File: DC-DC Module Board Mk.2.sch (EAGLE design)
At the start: 50 parts, among them J1 AVR_ICSP, P1 87833-04_S, Q1 SUM90P10-19L, Q2 ASFL1, Q3 MMBT540LT1SMD, U1 ATMEGA168, U2 CHB350, U4 LTV816S, X1 5566-2, X2 5566-2, X3 5566-2

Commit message: updated brick board to new half brick
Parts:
- removed C15, C16: 10nF, resistor:C-USC0603
- removed C17, C18, C21: 100nF, resistor:C-USC0603
- removed FB1: (no value), microbuilder:FERRITE
- removed J1: AVR_ICSP, SparkFun:AVR_SPI_PRG_62X3_LOCK
- removed LED5: YELLOW, SparkFun:LED0603
- removed LED6: GREEN, SparkFun:LED0603
- removed LED7: BLUE, SparkFun:LED0603
- removed Q2: ASFL1, crystal:ASFL1
- removed R15: 10k, resistor:R-US_R0603
- removed R16, R17, R18: 350, resistor:R-US_R0603
- removed R19, R20: 3.3k, resistor:R-US_R0603
- removed R21: 10k, pot:TRIM_US-SM-42/43W
- removed S1: (no value), SparkFun:TAC_SWITCHSMD
- removed U1: ATMEGA168, SparkFun:ATMEGA168
- removed U2: CHB350, Custom_Components:CHB350-24V
- added U$1: BRICK_DC-DC_CONVERTER, PowerComponents:BRICK_DC-DC_CONVERTER
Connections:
- removed net A0: U1.PD0(RXD)
- removed net A1: U1.PD1(TXD)
- removed net A2: U1.PD2(INT0)
- removed net AREF: C16.1, U1.AREF
- removed net CLK: Q2.FO, U1.PB6(XTAL1/TOSC1)
- removed net I24_MEA: U1.PC3(ADC3)
- removed net MISO: J1.1, U1.PB4(MISO)
- removed net MOSI: J1.4, U1.PB3(MOSI/OC2)
- removed net N$16: FB1.P$2, U1.AVCC
- removed net N$19: R21.S, U2.TRIM
- removed net N$20: LED5.A, R16.1
- removed net N$21: LED6.A, R17.1
- removed net N$25: LED7.A, R18.1
- removed net RST: C15.1, J1.5, R15.1, S1.3, S1.4, U1.PC6(/RESET)
- removed net SCK: J1.3, U1.PB5(SCK)
- removed net TEMP_OUT: U1.PC2(ADC2)
- removed net TEST1: R16.2, U1.PD5(T1)
- removed net TEST2: R17.2, U1.PD6(AIN0)
- removed net TEST3: R18.2, U1.PD7(AIN1)
- removed net V24_MEA: U1.PC0(ADC0)
- net +5V: no longer C17.1, C18.1, C21.1, FB1.P$1, J1.2, Q2.VCC, R15.2, R19.2, R20.2, U1.VCC@1, U1.VCC@2
- net EN: no longer U2.EN
- net ENABLE: no longer U1.PD4(XCK/T0)
- net GND: now also U$1.-S, U$1.-VOUT; no longer C15.2, C16.2, C17.2, C18.2, C21.2, J1.6, LED5.C, LED6.C, LED7.C, Q2.GND, R21.E, S1.1, S1.2, U1.AGND, U1.GND@1, U1.GND@2, U2.GND, U2.SENSE-
- net GND1: now also U$1.-VIN; no longer U2.VIN-
- net N$6: now also U$1.+VIN; no longer U2.VIN+
- net SCL: no longer R19.1, U1.PC5(ADC5/SCL)
- net SDA: no longer R20.1, U1.PC4(ADC4/SDA)
- net V+: now also U$1.+S, U$1.+VOUT; no longer R21.A, U2.SENSE+, U2.VOUT
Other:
- note removed: "C:/Users/Clayton Kleppinger/Dropbox/IEEE ROV 2012/Electronics/DC-DC Module Board/purdue-logo.bmp"

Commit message: addressing and labels
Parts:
- removed C13, C19: 100nF, resistor:C-USC0603
- removed P1: 87833-04_S, con-molex-milli-grid:87833-04_S
- removed Q3: MMBT540LT1SMD, transistor-pnp:MMBT540LT1SMD
- removed R1: 1k, resistor:R-US_R0603
- removed R22, R23, R24: 10k, resistor:R-US_R0603
- removed U4: LTV816S, optocoupler:LTV816S
- removed X1, X2, X3: 5566-2, con-molex:5566-2
- added R5, R7: 10, resistor:R-US_R0603
- added R6: 0, resistor:R-US_R0603
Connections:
- removed net +24V: C19.1, X2-2.S, X3-2.S
- removed net +5V: P1-3.P
- removed net EN: R22.1, R24.1
- removed net ENABLE: R1.1
- removed net N$22: Q3.C, R24.2
- removed net N$23: R23.1, U4.COL
- removed net N$24: Q3.B, R23.2
- new net ADRS00A: R7.2, U$1.SA0
- new net ADRS00B: R5.2, U$1.SA1
- new net ALERT: U$1.SMBALERT
- new net PG: U$1.PG
- net GND: now also R5.1, R7.1; no longer C19.2, P1-4.P, U4.C, X2-1.S, X3-1.S
- net GND1: now also R6.1; no longer C13.2, R22.2, U4.EMIT, X1-1.S
- net N$1: now also R6.2, U$1.ON/OFF1; no longer R1.2, U4.A
- net N$6: no longer Q3.E
- net SCL: now also U$1.SCL; no longer P1-1.P
- net SDA: now also U$1.SDA; no longer P1-2.P
- net VCC: no longer C13.1, X1-2.S
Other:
- note added: "address 00"

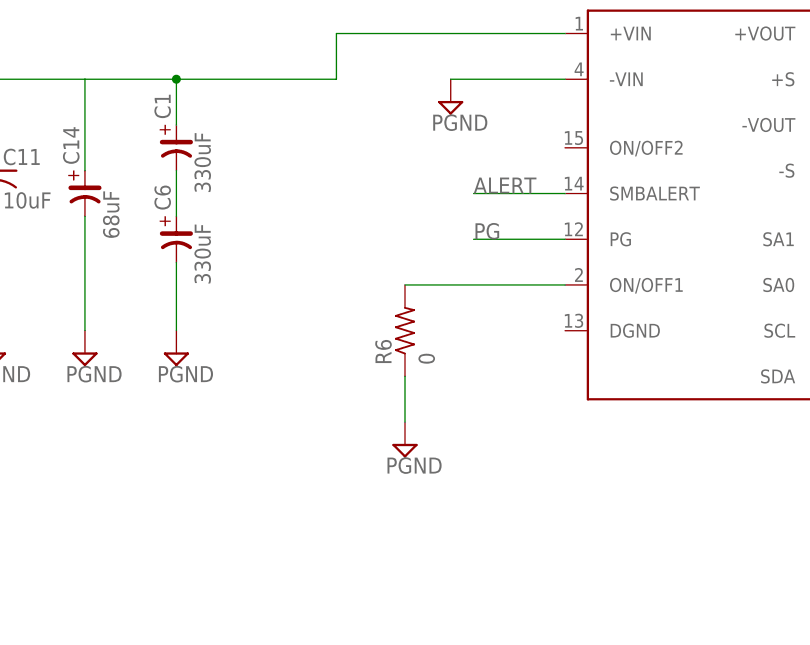
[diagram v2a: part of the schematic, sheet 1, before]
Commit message: added LEDs to smbalert and pg
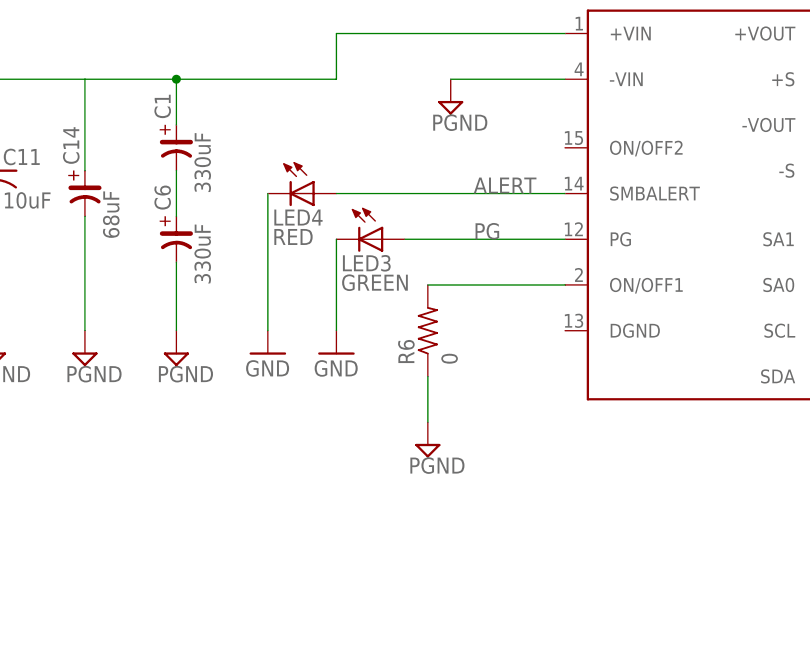
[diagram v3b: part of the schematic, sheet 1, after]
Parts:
- added LED3: GREEN, SparkFun:LED0603
- added LED4: RED, SparkFun:LED0603
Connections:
- net ALERT: now also LED4.A
- net GND: now also LED3.C, LED4.C
- net PG: now also LED3.A
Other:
- moved on the sheet: R6
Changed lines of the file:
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@@
 <attribute name="PARTNO" value="1.00MHCT-ND"/>
 </part>
+<part name="LED3" library="SparkFun" deviceset="LED" device="0603" value="GREEN">
+<attribute name="BOM" value="INCLUDE"/>
+<attribute name="PARTNO" value="160-1446-1-ND"/>
+</part>
+<part name="LED4" library="SparkFun" deviceset="LED" device="0603" value="RED">
+<attribute name="BOM" value="INCLUDE"/>
+<attribute name="PARTNO" value="160-1446-1-ND"/>
+</part>
+<part name="GND5" library="supply1" deviceset="GND" device=""/>
+<part name="GND6" library="supply1" deviceset="GND" device=""/>
 </parts>
 <sheets>
@@
 <instance part="GND2" gate="1" x="160.02" y="114.3"/>
 <instance part="U$1" gate="G$1" x="129.54" y="124.46"/>
-<instance part="SUPPLY7" gate="G$1" x="96.52" y="86.36"/>
+<instance part="SUPPLY7" gate="G$1" x="99.06" y="86.36"/>
 <instance part="GND1" gate="1" x="180.34" y="86.36"/>
 <instance part="R5" gate="G$1" x="180.34" y="99.06" rot="R90">
@@
 <attribute name="BOM" value="INCLUDE" x="180.34" y="99.06" size="0.0254" layer="96" font="vector" display="off"/>
 </instance>
-<instance part="R6" gate="G$1" x="96.52" y="99.06" rot="R90">
-<attribute name="PARTNO" value="1.00MHCT-ND" x="96.52" y="99.06" size="0.0254" layer="96" font="vector" display="off"/>
-<attribute name="BOM" value="INCLUDE" x="96.52" y="99.06" size="0.0254" layer="96" font="vector" display="off"/>
+<instance part="R6" gate="G$1" x="99.06" y="99.06" rot="R90">
+<attribute name="PARTNO" value="1.00MHCT-ND" x="99.06" y="99.06" size="0.0254" layer="96" font="vector" display="off"/>
+<attribute name="BOM" value="INCLUDE" x="99.06" y="99.06" size="0.0254" layer="96" font="vector" display="off"/>
 </instance>
 <instance part="R7" gate="G$1" x="167.64" y="99.06" rot="R90">
@@
 <attribute name="BOM" value="INCLUDE" x="167.64" y="99.06" size="0.0254" layer="96" font="vector" display="off"/>
 </instance>
+<instance part="LED3" gate="G$1" x="93.98" y="109.22" rot="R270">
+<attribute name="PARTNO" value="160-1446-1-ND" x="93.98" y="109.22" size="0.0254" layer="96" font="vector" rot="R270" display="off"/>
+<attribute name="BOM" value="INCLUDE" x="93.98" y="109.22" size="0.0254" layer="96" font="vector" rot="R270" display="off"/>
+</instance>
+<instance part="LED4" gate="G$1" x="86.36" y="114.3" rot="R270">
+<attribute name="PARTNO" value="160-1446-1-ND" x="86.36" y="114.3" size="0.0254" layer="96" font="vector" rot="R270" display="off"/>
+<attribute name="BOM" value="INCLUDE" x="86.36" y="114.3" size="0.0254" layer="96" font="vector" rot="R270" display="off"/>
+</instance>
+<instance part="GND5" gate="1" x="81.28" y="96.52"/>
+<instance part="GND6" gate="1" x="88.9" y="96.52"/>
 </instances>
 <busses>
@@
 <junction x="180.34" y="93.98"/>
 <pinref part="R7" gate="G$1" pin="1"/>
+</segment>
+<segment>
+<pinref part="LED4" gate="G$1" pin="C"/>
+<wire x1="81.28" y1="114.3" x2="81.28" y2="99.06" width="0.1524" layer="91"/>
+<pinref part="GND5" gate="1" pin="GND"/>
+</segment>
+<segment>
+<pinref part="LED3" gate="G$1" pin="C"/>
+<wire x1="88.9" y1="109.22" x2="88.9" y2="99.06" width="0.1524" layer="91"/>
+<pinref part="GND6" gate="1" pin="GND"/>
 </segment>
 </net>
@@
 <segment>
 <pinref part="SUPPLY7" gate="G$1" pin="GND1"/>
-<wire x1="96.52" y1="93.98" x2="96.52" y2="88.9" width="0.1524" layer="91"/>
+<wire x1="99.06" y1="93.98" x2="99.06" y2="88.9" width="0.1524" layer="91"/>
 <pinref part="R6" gate="G$1" pin="1"/>
 </segment>
@@
 <segment>
 <pinref part="U$1" gate="G$1" pin="ON/OFF1"/>
-<wire x1="114.3" y1="104.14" x2="96.52" y2="104.14" width="0.1524" layer="91"/>
+<wire x1="114.3" y1="104.14" x2="99.06" y2="104.14" width="0.1524" layer="91"/>
 <pinref part="R6" gate="G$1" pin="2"/>
 </segment>
@@
 <segment>
 <pinref part="U$1" gate="G$1" pin="SMBALERT"/>
-<wire x1="114.3" y1="114.3" x2="104.14" y2="114.3" width="0.1524" layer="91"/>
 <label x="104.14" y="114.3" size="1.778" layer="95"/>
+<pinref part="LED4" gate="G$1" pin="A"/>
+<wire x1="114.3" y1="114.3" x2="88.9" y2="114.3" width="0.1524" layer="91"/>
 </segment>
 </net>
@@
 <segment>
 <pinref part="U$1" gate="G$1" pin="PG"/>
-<wire x1="114.3" y1="109.22" x2="104.14" y2="109.22" width="0.1524" layer="91"/>
+<wire x1="114.3" y1="109.22" x2="96.52" y2="109.22" width="0.1524" layer="91"/>
 <label x="104.14" y="109.22" size="1.778" layer="95"/>
-</segment>
-</net>
+<pinref part="LED3" gate="G$1" pin="A"/>
+</segment>
+</net>

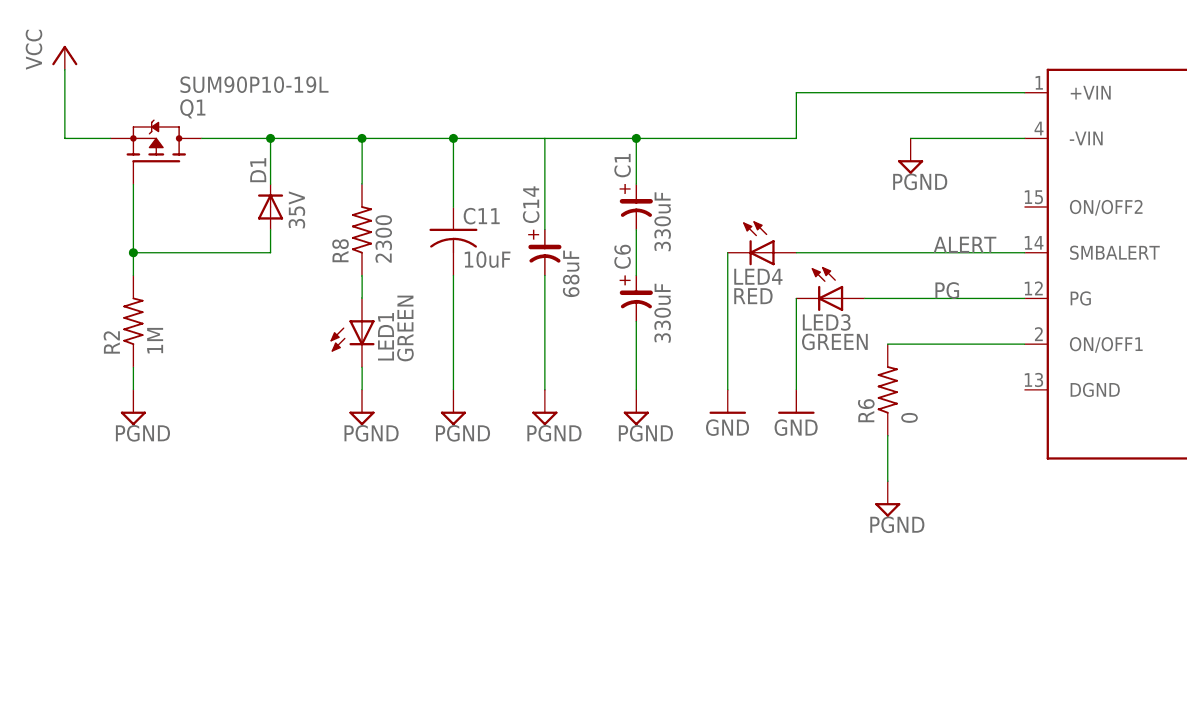
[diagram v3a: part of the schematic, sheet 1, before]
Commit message: changed PGND to GND
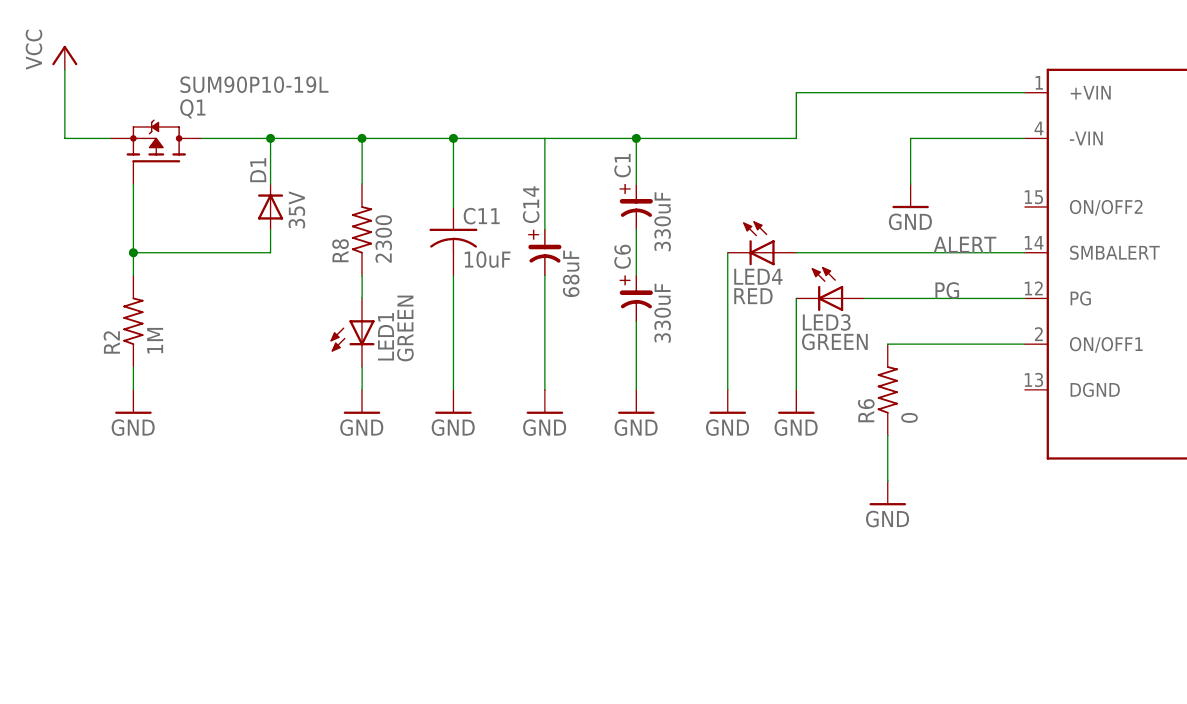
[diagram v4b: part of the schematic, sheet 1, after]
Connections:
- removed net GND1: C11.2, C14.-, C6.-, LED1.C, R2.1, R6.1, U$1.-VIN
- net GND: now also C11.2, C14.-, C6.-, LED1.C, R2.1, R6.1, U$1.-VIN
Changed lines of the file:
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@@
 <attribute name="PARTNO" value="SUM90P10-19L-E3CT-ND"/>
 </part>
-<part name="SUPPLY1" library="supply2" deviceset="GND1" device="" value="PGND"/>
-<part name="SUPPLY2" library="supply2" deviceset="GND1" device="" value="PGND"/>
-<part name="SUPPLY3" library="supply2" deviceset="GND1" device="" value="PGND"/>
-<part name="SUPPLY4" library="supply2" deviceset="GND1" device="" value="PGND"/>
-<part name="SUPPLY5" library="supply2" deviceset="GND1" device="" value="PGND"/>
 <part name="C22" library="SparkFun" deviceset="CAP_POL" device="7343" value="10uF">
 <attribute name="BOM" value="INCLUDE"/>
@@
 </part>
 <part name="GND40" library="supply1" deviceset="GND" device=""/>
-<part name="SUPPLY6" library="supply2" deviceset="GND1" device="" value="PGND"/>
 <part name="GND2" library="supply1" deviceset="GND" device=""/>
 <part name="U$1" library="PowerComponents" deviceset="BRICK_DC-DC_CONVERTER" device=""/>
-<part name="SUPPLY7" library="supply2" deviceset="GND1" device="" value="PGND"/>
 <part name="GND1" library="supply1" deviceset="GND" device=""/>
 <part name="R5" library="resistor" deviceset="R-US_" device="R0603" value="10">
@@
 <part name="GND5" library="supply1" deviceset="GND" device=""/>
 <part name="GND6" library="supply1" deviceset="GND" device=""/>
+<part name="GND7" library="supply1" deviceset="GND" device=""/>
+<part name="GND8" library="supply1" deviceset="GND" device=""/>
+<part name="GND9" library="supply1" deviceset="GND" device=""/>
+<part name="GND10" library="supply1" deviceset="GND" device=""/>
+<part name="GND11" library="supply1" deviceset="GND" device=""/>
+<part name="GND12" library="supply1" deviceset="GND" device=""/>
+<part name="GND13" library="supply1" deviceset="GND" device=""/>
 </parts>
 <sheets>
@@
 <attribute name="BOM" value="INCLUDE" x="17.78" y="124.46" size="0.0254" layer="96" font="vector" display="off"/>
 </instance>
-<instance part="SUPPLY1" gate="G$1" x="15.24" y="96.52"/>
-<instance part="SUPPLY2" gate="G$1" x="40.64" y="96.52"/>
-<instance part="SUPPLY3" gate="G$1" x="50.8" y="96.52"/>
-<instance part="SUPPLY4" gate="G$1" x="60.96" y="96.52"/>
-<instance part="SUPPLY5" gate="G$1" x="71.12" y="96.52"/>
 <instance part="C22" gate="G$1" x="208.28" y="114.3">
 <attribute name="PARTNO" value="399-3893-1-ND" x="208.28" y="114.3" size="1.778" layer="96" display="off"/>
@@
 </instance>
 <instance part="GND40" gate="1" x="228.6" y="96.52"/>
-<instance part="SUPPLY6" gate="G$1" x="101.6" y="124.46"/>
 <instance part="GND2" gate="1" x="160.02" y="114.3"/>
 <instance part="U$1" gate="G$1" x="129.54" y="124.46"/>
-<instance part="SUPPLY7" gate="G$1" x="99.06" y="86.36"/>
 <instance part="GND1" gate="1" x="180.34" y="86.36"/>
 <instance part="R5" gate="G$1" x="180.34" y="99.06" rot="R90">
@@
 <instance part="GND5" gate="1" x="81.28" y="96.52"/>
 <instance part="GND6" gate="1" x="88.9" y="96.52"/>
+<instance part="GND7" gate="1" x="71.12" y="96.52"/>
+<instance part="GND8" gate="1" x="60.96" y="96.52"/>
+<instance part="GND9" gate="1" x="50.8" y="96.52"/>
+<instance part="GND10" gate="1" x="40.64" y="96.52"/>
+<instance part="GND11" gate="1" x="15.24" y="96.52"/>
+<instance part="GND12" gate="1" x="99.06" y="86.36"/>
+<instance part="GND13" gate="1" x="101.6" y="119.38"/>
 </instances>
 <busses>
@@
 <wire x1="88.9" y1="109.22" x2="88.9" y2="99.06" width="0.1524" layer="91"/>
 <pinref part="GND6" gate="1" pin="GND"/>
+</segment>
+<segment>
+<pinref part="C6" gate="G$1" pin="-"/>
+<wire x1="71.12" y1="106.68" x2="71.12" y2="99.06" width="0.1524" layer="91"/>
+<pinref part="GND7" gate="1" pin="GND"/>
+</segment>
+<segment>
+<pinref part="C14" gate="G$1" pin="-"/>
+<wire x1="60.96" y1="111.76" x2="60.96" y2="99.06" width="0.1524" layer="91"/>
+<pinref part="GND8" gate="1" pin="GND"/>
+</segment>
+<segment>
+<pinref part="C11" gate="G$1" pin="2"/>
+<wire x1="50.8" y1="111.76" x2="50.8" y2="99.06" width="0.1524" layer="91"/>
+<pinref part="GND9" gate="1" pin="GND"/>
+</segment>
+<segment>
+<pinref part="LED1" gate="G$1" pin="C"/>
+<wire x1="40.64" y1="101.6" x2="40.64" y2="99.06" width="0.1524" layer="91"/>
+<pinref part="GND10" gate="1" pin="GND"/>
+</segment>
+<segment>
+<pinref part="R2" gate="G$1" pin="1"/>
+<wire x1="15.24" y1="101.6" x2="15.24" y2="99.06" width="0.1524" layer="91"/>
+<pinref part="GND11" gate="1" pin="GND"/>
+</segment>
+<segment>
+<wire x1="99.06" y1="93.98" x2="99.06" y2="88.9" width="0.1524" layer="91"/>
+<pinref part="R6" gate="G$1" pin="1"/>
+<pinref part="GND12" gate="1" pin="GND"/>
+</segment>
+<segment>
+<pinref part="U$1" gate="G$1" pin="-VIN"/>
+<pinref part="GND13" gate="1" pin="GND"/>
+<wire x1="114.3" y1="127" x2="101.6" y2="127" width="0.1524" layer="91"/>
+<wire x1="101.6" y1="127" x2="101.6" y2="121.92" width="0.1524" layer="91"/>
 </segment>
 </net>
@@
 </segment>
 </net>
-<net name="GND1" class="0">
-<segment>
-<pinref part="R2" gate="G$1" pin="1"/>
-<wire x1="15.24" y1="101.6" x2="15.24" y2="99.06" width="0.1524" layer="91"/>
-<pinref part="SUPPLY1" gate="G$1" pin="GND1"/>
-</segment>
-<segment>
-<pinref part="LED1" gate="G$1" pin="C"/>
-<wire x1="40.64" y1="101.6" x2="40.64" y2="99.06" width="0.1524" layer="91"/>
-<pinref part="SUPPLY2" gate="G$1" pin="GND1"/>
-</segment>
-<segment>
-<pinref part="C11" gate="G$1" pin="2"/>
-<wire x1="50.8" y1="111.76" x2="50.8" y2="99.06" width="0.1524" layer="91"/>
-<pinref part="SUPPLY3" gate="G$1" pin="GND1"/>
-</segment>
-<segment>
-<pinref part="C14" gate="G$1" pin="-"/>
-<wire x1="60.96" y1="111.76" x2="60.96" y2="99.06" width="0.1524" layer="91"/>
-<pinref part="SUPPLY4" gate="G$1" pin="GND1"/>
-</segment>
-<segment>
-<pinref part="C6" gate="G$1" pin="-"/>
-<wire x1="71.12" y1="106.68" x2="71.12" y2="99.06" width="0.1524" layer="91"/>
-<pinref part="SUPPLY5" gate="G$1" pin="GND1"/>
-</segment>
-<segment>
-<pinref part="SUPPLY6" gate="G$1" pin="GND1"/>
-<pinref part="U$1" gate="G$1" pin="-VIN"/>
-<wire x1="101.6" y1="127" x2="114.3" y2="127" width="0.1524" layer="91"/>
-</segment>
-<segment>
-<pinref part="SUPPLY7" gate="G$1" pin="GND1"/>
-<wire x1="99.06" y1="93.98" x2="99.06" y2="88.9" width="0.1524" layer="91"/>
-<pinref part="R6" gate="G$1" pin="1"/>
-</segment>
-</net>
